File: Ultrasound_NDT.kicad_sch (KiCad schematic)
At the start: 0 parts

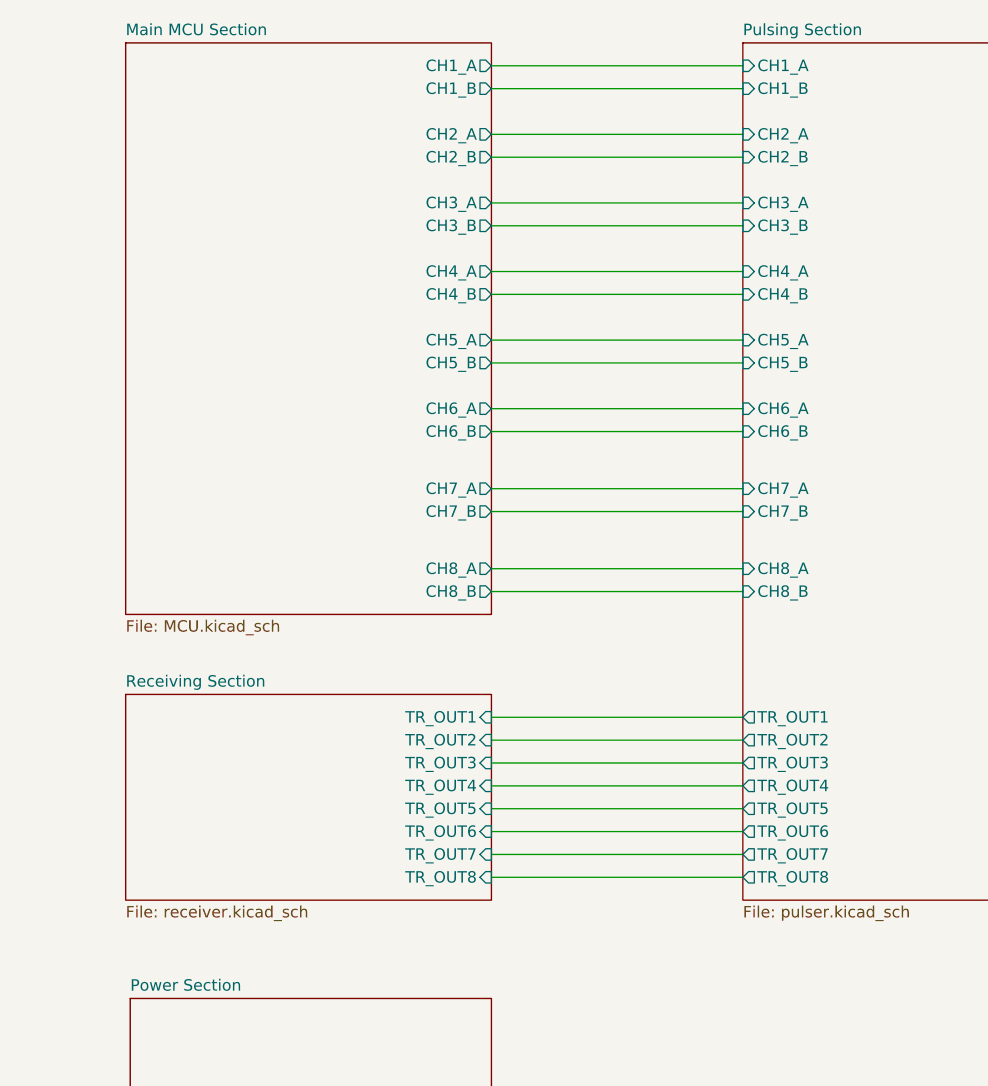
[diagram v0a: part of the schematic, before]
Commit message: converted diff signals to single-ended, modified pulser & MCU, power untouched
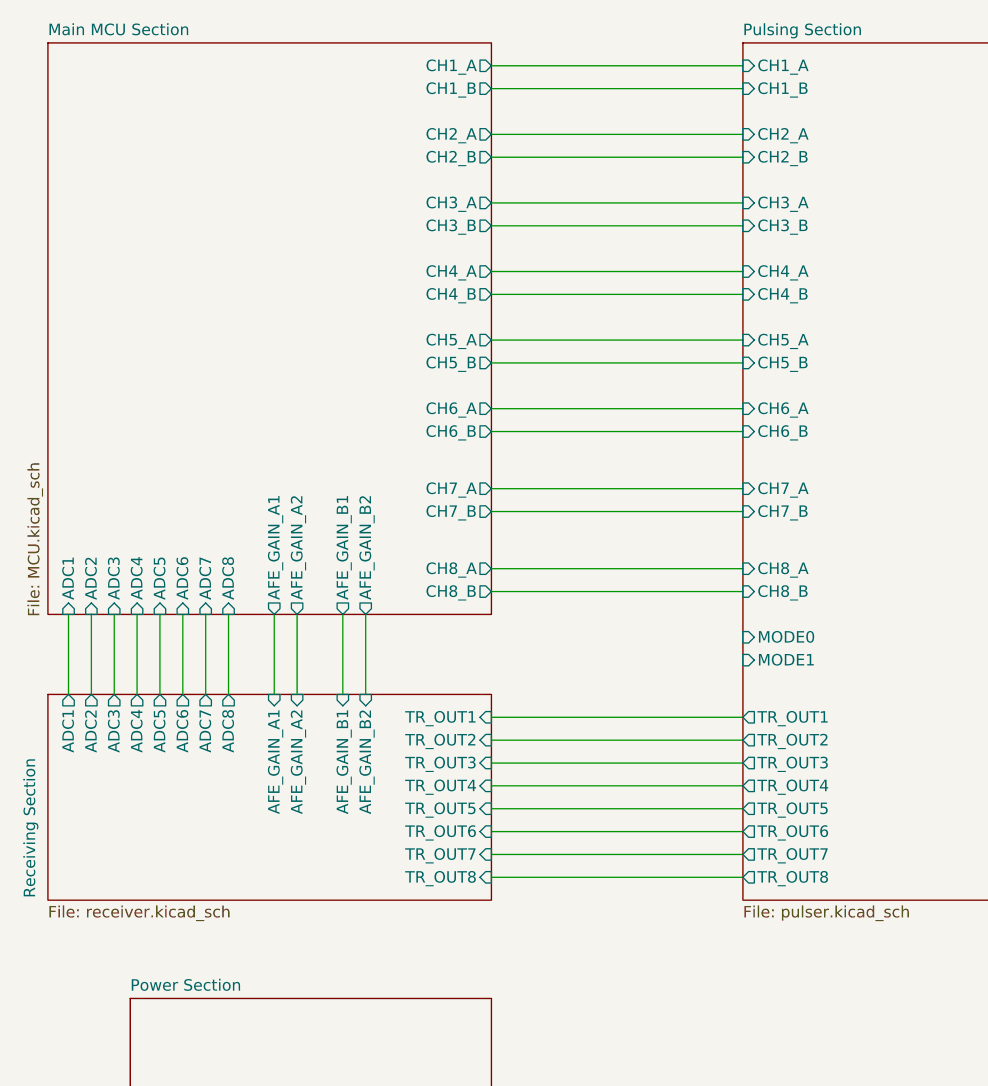
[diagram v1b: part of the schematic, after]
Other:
- sheet Main MCU Section ports: added ADC1, ADC2, ADC3, ADC4, ADC5, ADC6, ADC7, ADC8, AFE_GAIN_A1, AFE_GAIN_A2, AFE_GAIN_B1, AFE_GAIN_B2; removed none
- sheet Pulsing Section ports: added MODE0, MODE1; removed none
- sheet Receiving Section ports: added ADC1, ADC2, ADC3, ADC4, ADC5, ADC6, ADC7, ADC8, AFE_GAIN_A1, AFE_GAIN_A2, AFE_GAIN_B1, AFE_GAIN_B2; removed none

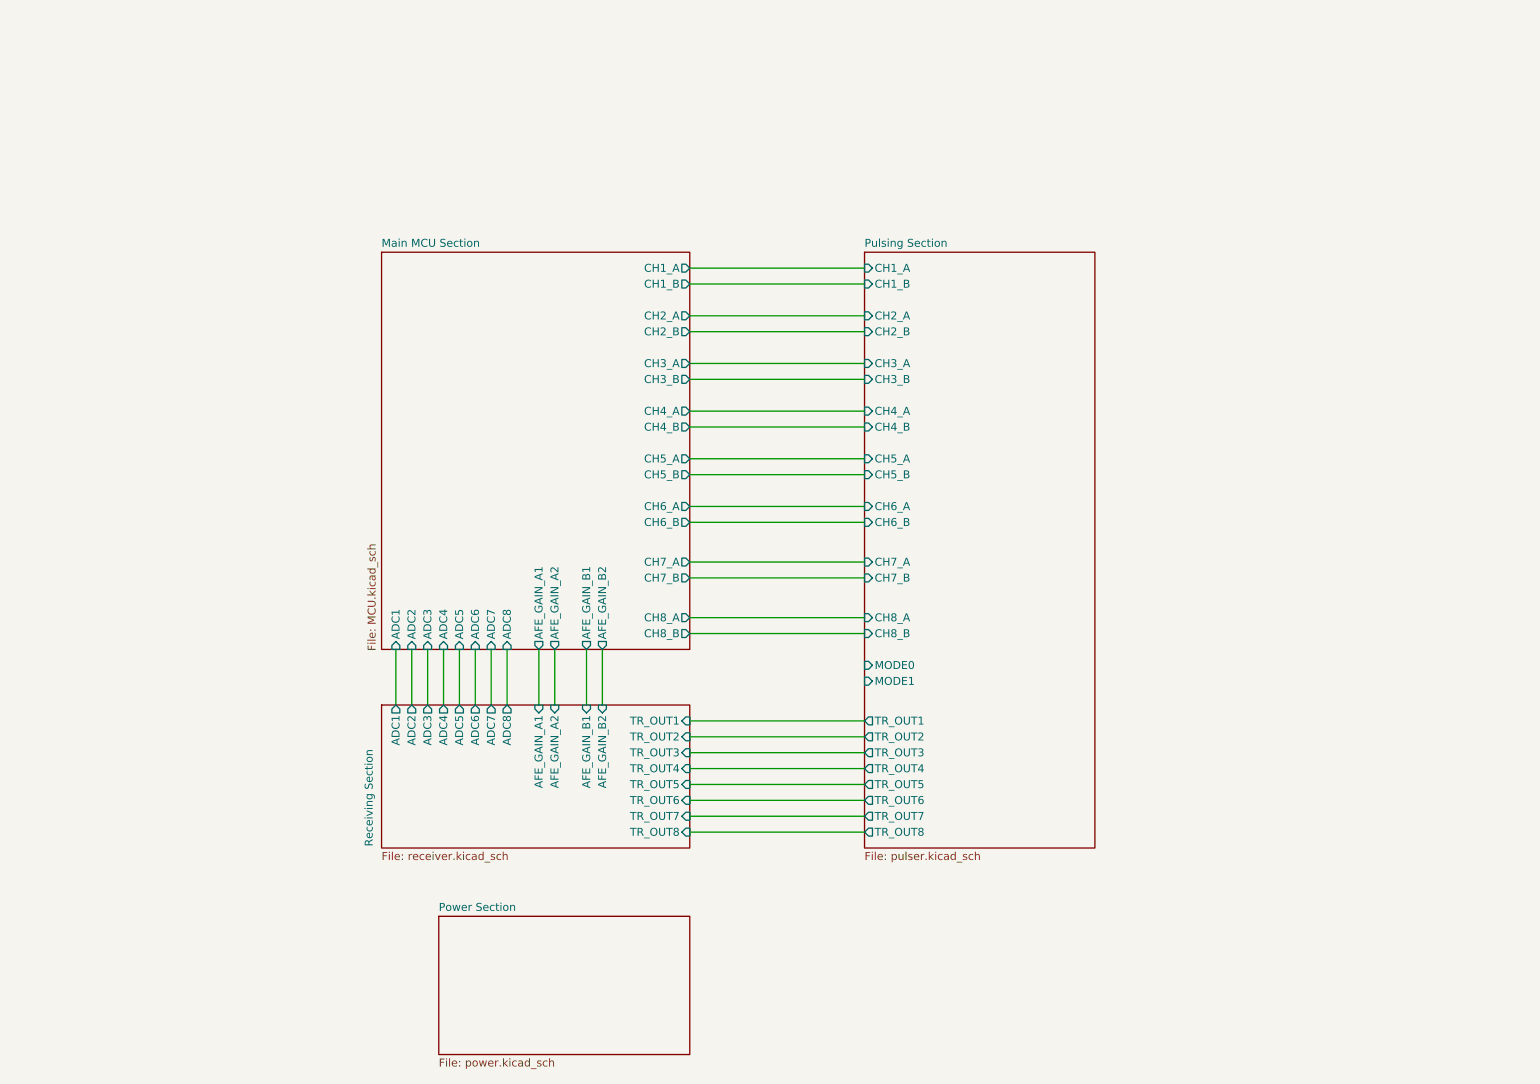
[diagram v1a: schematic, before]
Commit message: finished analog signal chain, added main power components, complete the schematic and form a power budget table
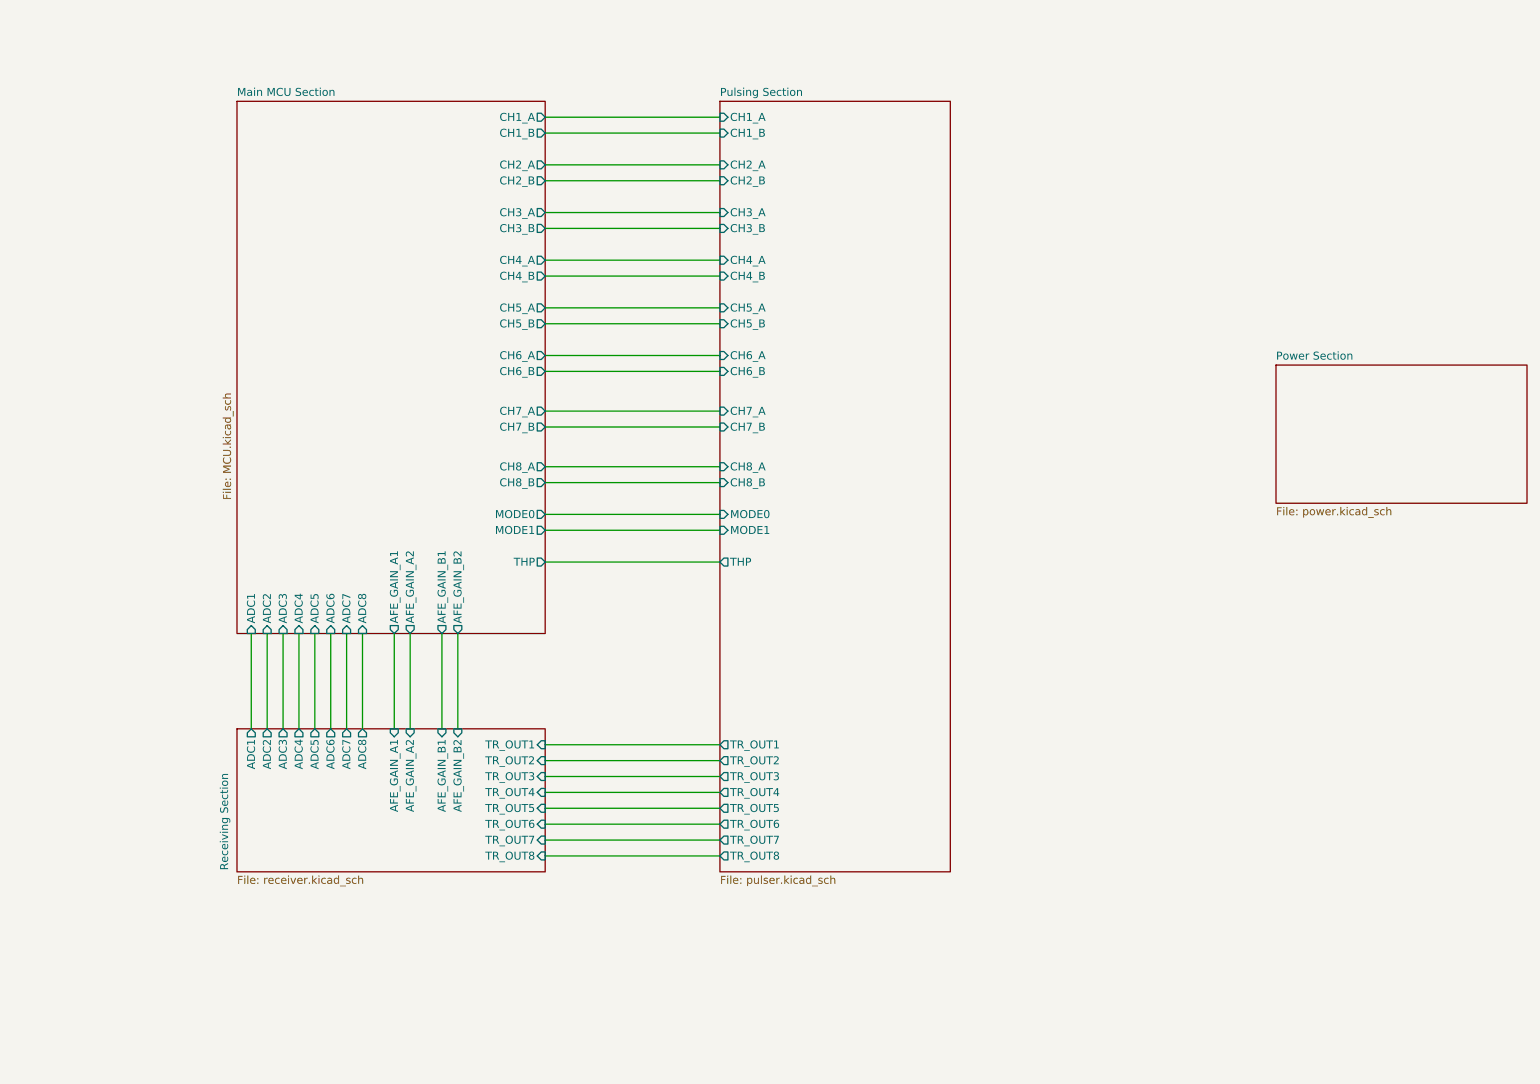
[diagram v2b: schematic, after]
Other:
- sheet Main MCU Section ports: added MODE0, MODE1, THP; removed none
- sheet Pulsing Section ports: added THP; removed none

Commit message: finished 50% of power section, 50% remaining + EEPROM & revision
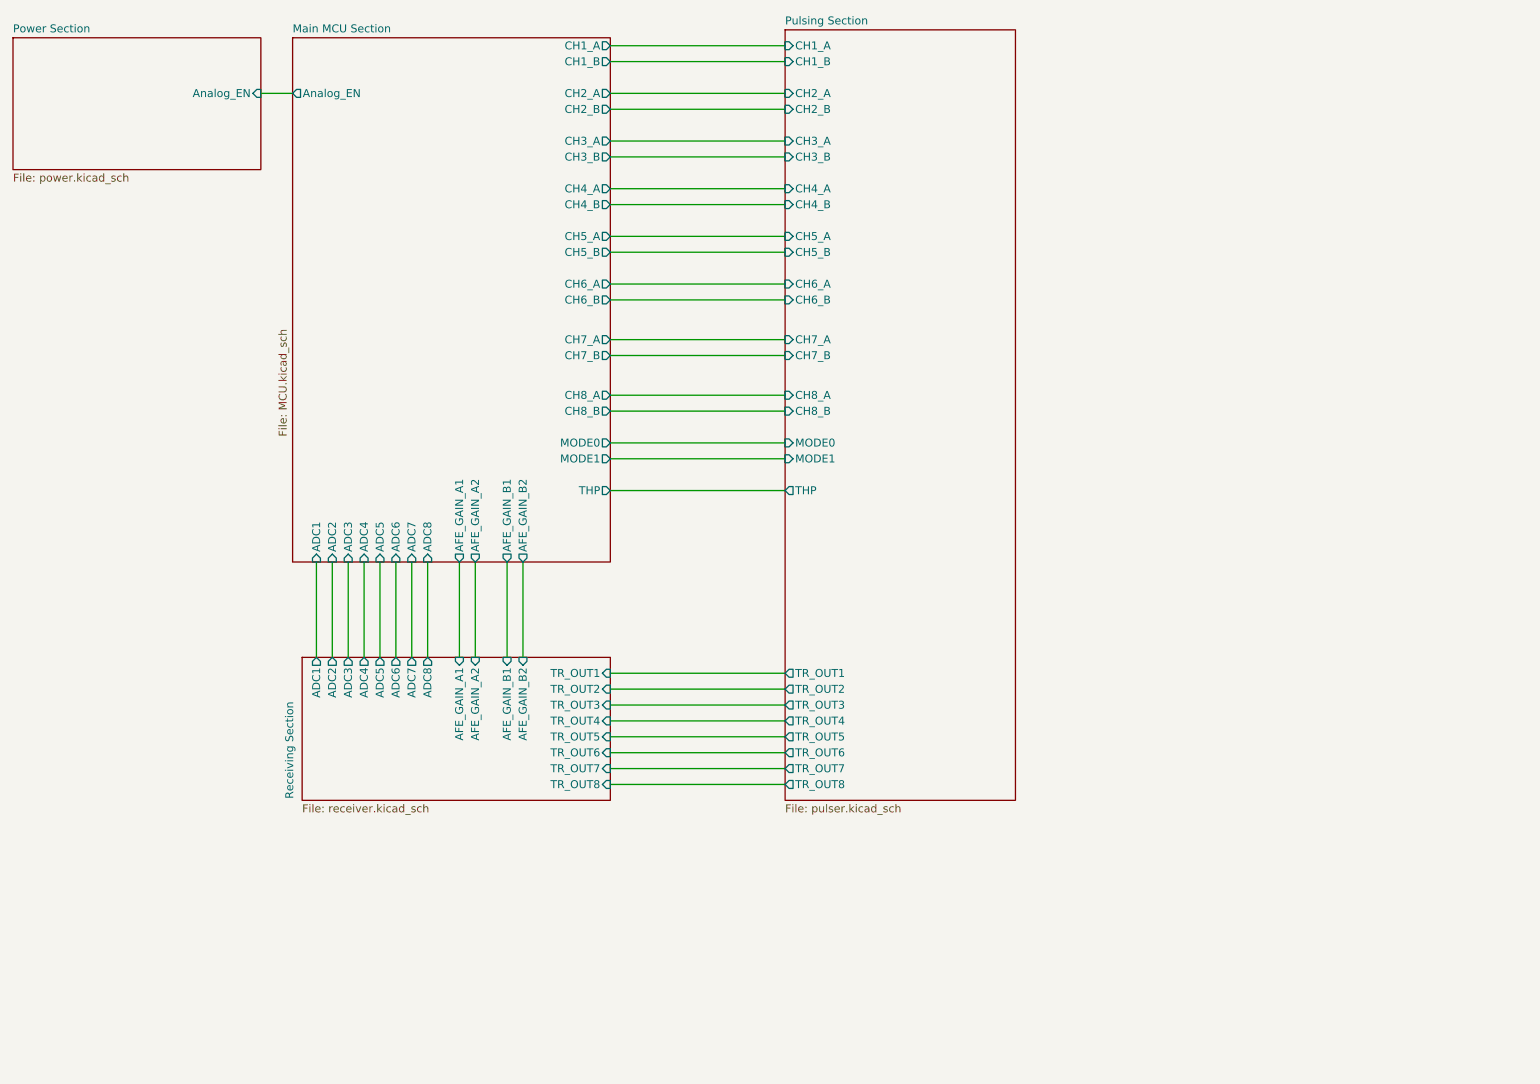
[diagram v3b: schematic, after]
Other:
- sheet Main MCU Section ports: added Analog_EN; removed none
- sheet Power Section ports: added Analog_EN; removed none

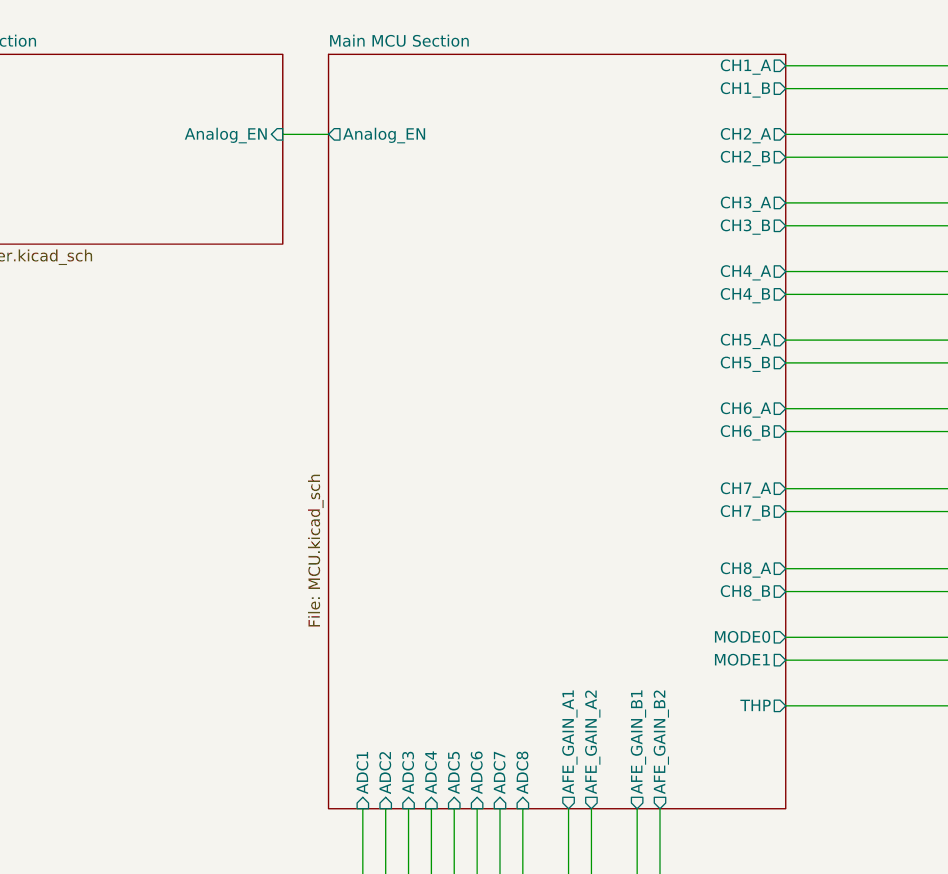
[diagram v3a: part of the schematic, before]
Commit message: 95% done, only headers for communication & power are remaining + RS232 transceiver & 1.5v reference
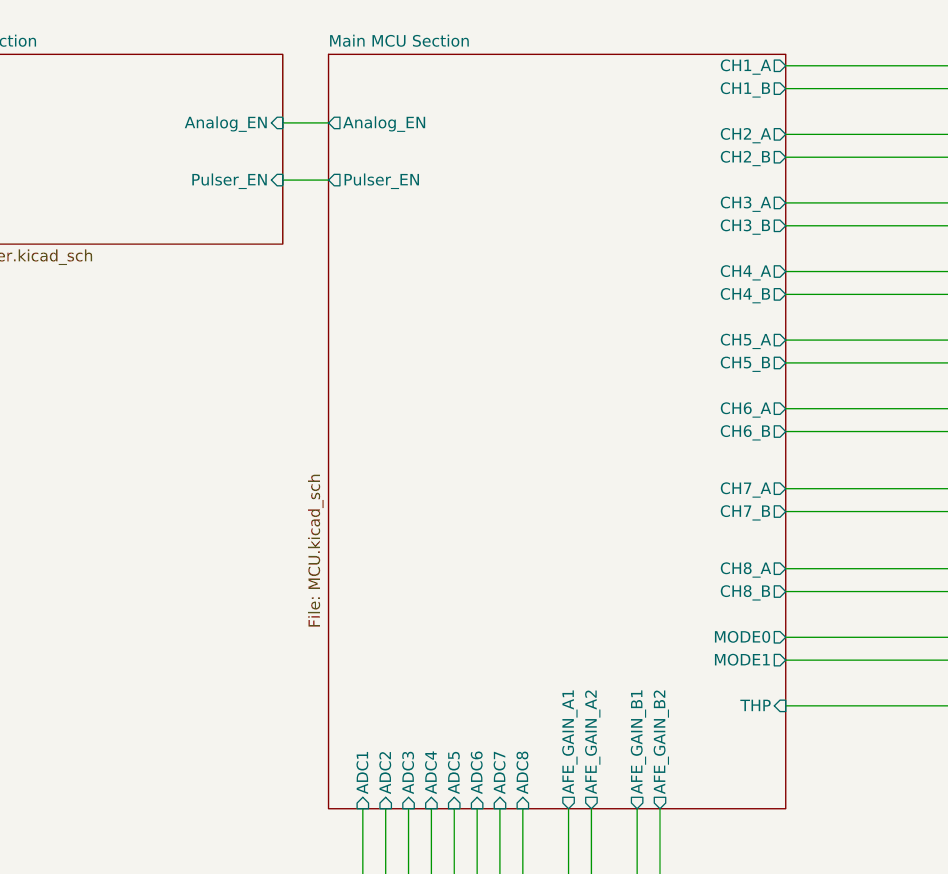
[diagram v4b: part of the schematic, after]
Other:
- sheet Main MCU Section ports: added Pulser_EN; removed none
- sheet Power Section ports: added Pulser_EN; removed none
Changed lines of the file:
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@@
 	(wire
 		(pts
-			(xy 53.34 29.21) (xy 58.42 29.21)
+			(xy 53.34 27.94) (xy 58.42 27.94)
 		)
 		(stroke
@@
 		(pts
 			(xy 62.23 104.14) (xy 62.23 119.38)
+		)
+		(stroke
+			(width 0)
+			(type default)
+		)
+	)
+	(wire
+		(pts
+			(xy 53.34 34.29) (xy 58.42 34.29)
 		)
 		(stroke
@@
 			)
 		)
-		(pin "THP" output
+		(pin "THP" input
 			(at 109.22 92.71 0)
 			(effects
@@
 		)
 		(pin "Analog_EN" output
-			(at 58.42 29.21 180)
+			(at 58.42 27.94 180)
+			(effects
+				(font
+					(size 1.27 1.27)
+				)
+				(justify left)
+			)
+		)
+		(pin "Pulser_EN" output
+			(at 58.42 34.29 180)
 			(effects
 				(font
@@
 		)
 		(pin "Analog_EN" input
-			(at 53.34 29.21 0)
-			(effects
-				(font
+			(at 53.34 27.94 0)
+			(effects
+				(font
+					(size 1.27 1.27)
+				)
+				(justify right)
+			)
+		)
+		(pin "Pulser_EN" input
+			(at 53.34 34.29 0)
+			(effects
+				(font
